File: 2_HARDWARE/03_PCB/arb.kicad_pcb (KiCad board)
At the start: 4 copper layers, 100 x 100 mm, 268 parts, among them J1 TYPE-C-31-M-12, J2 SMA, J3 SMA, J4 BNC, J5 PH-00244, SW1 TS-1187A-B-A-B, SW2 SS-12D02-VG4, SW3 SS-12D02-VG4, U1 TLV70333DBV, U10 LMK1C1103PWR, U11 STM32F446ZETx, U12 ICE40UP5K-SG48ITR, U13 93LC56BT-I_OT, U14 FT2232HL, U15 W25Q128JVSIQ, U16 W25Q128JVSIQ, U17 AD9850, U18 AD9744, U19 LM6171, U2 TLV76133DCY, U20 LM6171, U21 TMUX6104, U22 TPL0401B-10, U23 THS3491, U24 ADG1219BRJZ, U25 LM6171, U26 TMUX6104, U3 TLV70333DBV, U4 LM3880MF-1AA, U5 TLV70312DBV, U6 TLV70325DBV, U7 TPS65131RGE, U8 TPD2E001DRL, U9 ADG1219BRJZ, X1 ASE-10.000MHz, X2 ASE-100.000MHz, Y1 32.768k, Y2 12 MHz

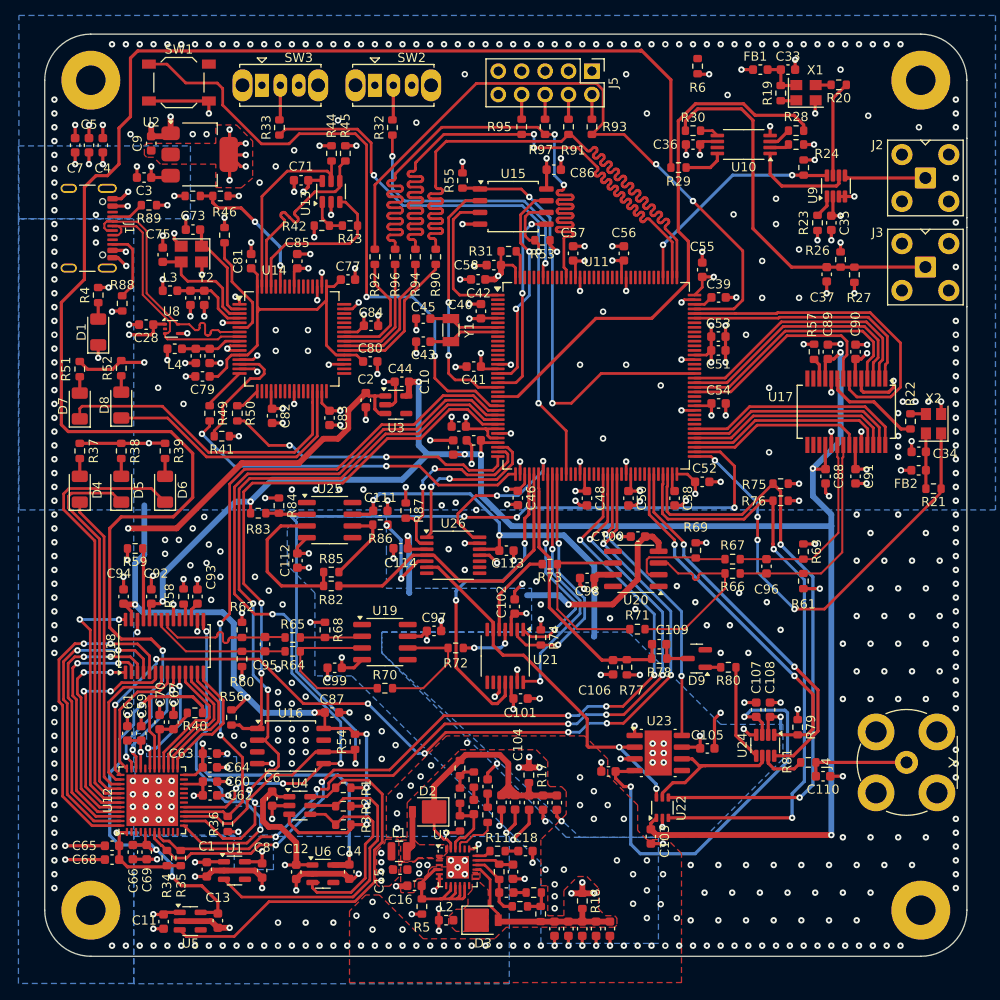
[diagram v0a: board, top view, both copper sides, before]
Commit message: FEAT: Added silkscreen.
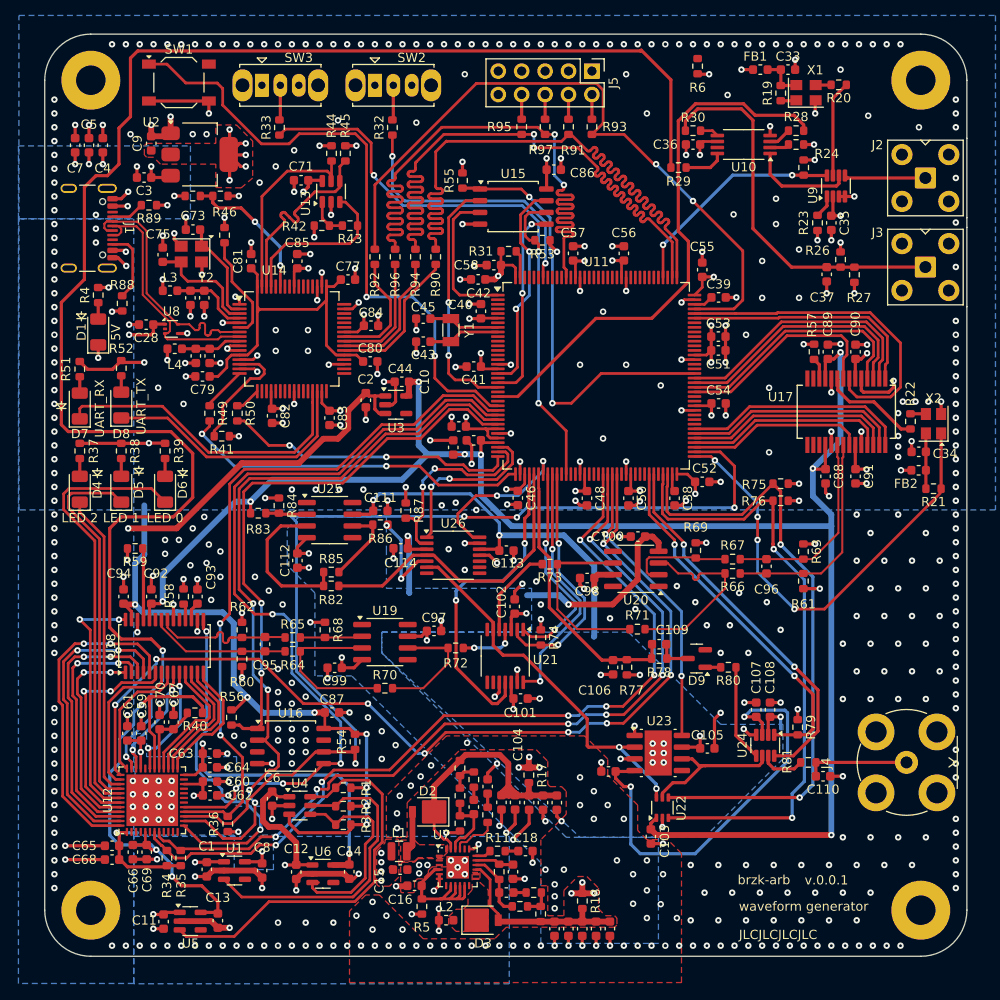
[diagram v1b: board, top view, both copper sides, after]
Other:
- board text added: "5V"
- board text added: "JLCJLCJLCJLC"
- board text added: "LED 0"
- board text added: "LED 1"
- board text added: "LED 2"
- board text added: "UART_RX"
- board text added: "UART_TX"
- board text added: "brzk-arb"
- board text added: "v.0.0.1"
- board text added: "waveform generator"

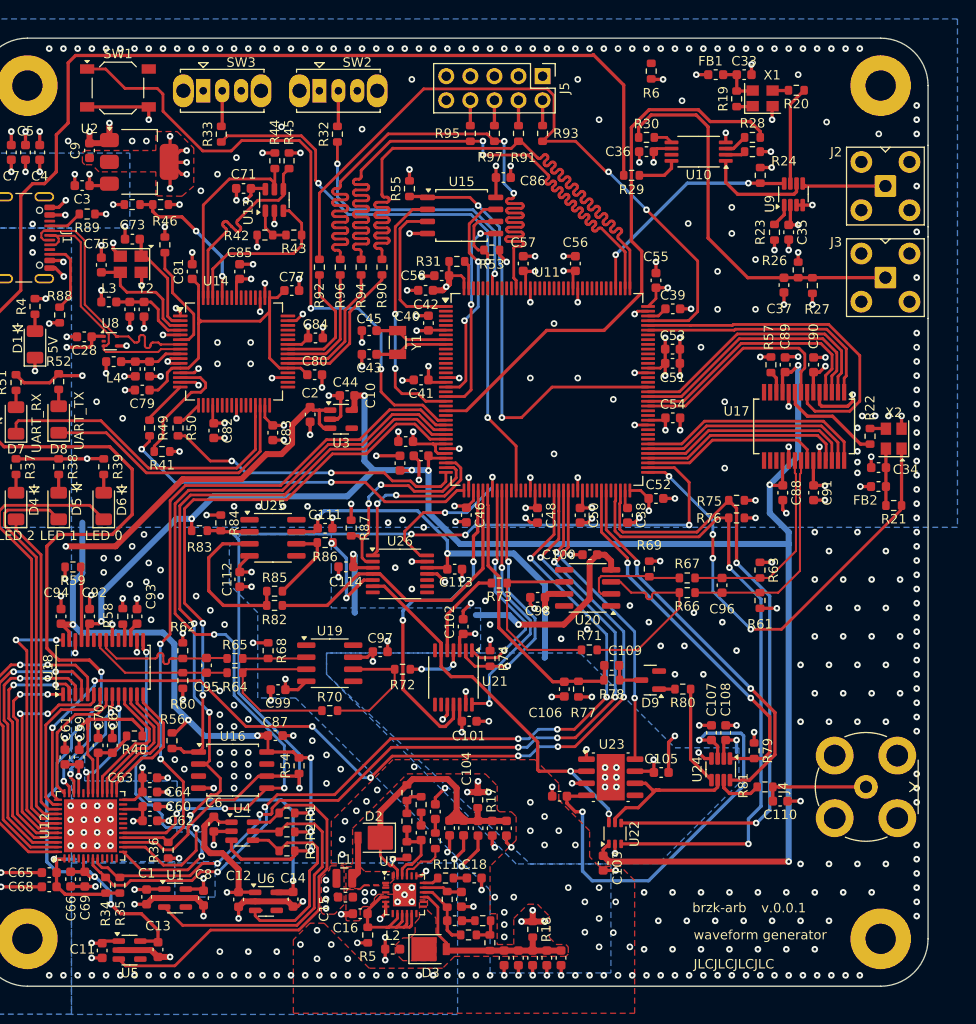
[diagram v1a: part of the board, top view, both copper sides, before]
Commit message: MINOR: Adjusted soldermask and ported Schematic + PCB to Kicad 9.0.
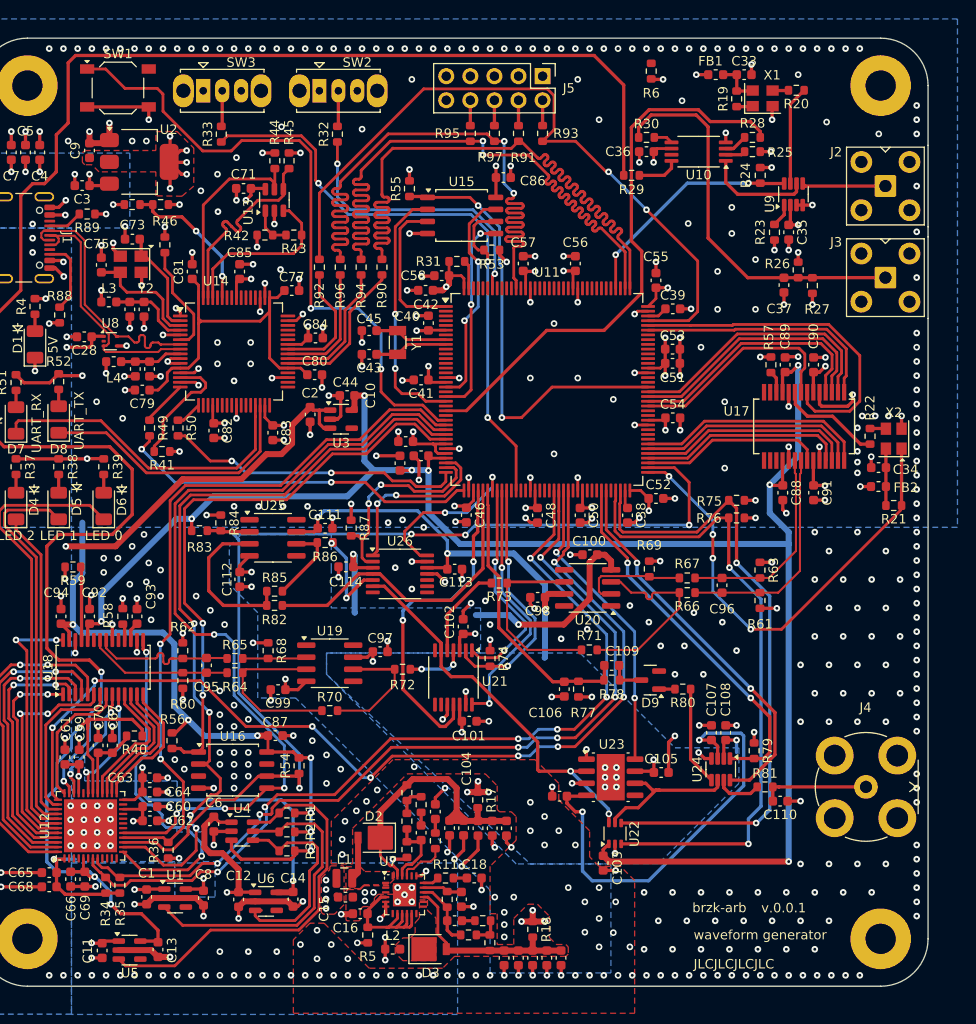
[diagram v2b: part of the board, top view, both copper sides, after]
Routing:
- net GND: vias 613 -> 616

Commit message: MINOR: Initial Reduced Size Analysis, need to make the board larger.
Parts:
- J2, J3, J4, U11: moved to B.Cu
- moved C1 351.3 mm to (-231.4, 99.1)
- moved C10 351.3 mm to (-210.2, 46.2)
- moved C100 351.3 mm to (-184.6, 63.0)
- moved C101 351.3 mm to (-197.3, 80.5)
- moved C102 351.3 mm to (-198.0, 70.6)
- moved C103 351.3 mm to (-183.2, 95.5)
- moved C104 351.3 mm to (-187.8, 88.5)
- moved C105 351.3 mm to (-177.1, 86.0)
- moved C106 351.3 mm to (-187.3, 77.2)
- moved C107 351.3 mm to (-171.8, 81.8)
- moved C108 351.3 mm to (-170.3, 81.8)
- moved C109 351.3 mm to (-182.3, 74.7)
- moved C11 351.3 mm to (-236.1, 104.7)
- moved C110 351.3 mm to (-164.6, 89.0)
- moved C111 351.3 mm to (-212.6, 60.2)
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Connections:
- J1 pad A1: GND -> (no net)
- J1 pad A12: GND -> (no net)
- J1 pad A4: 5P0V -> (no net)
- J1 pad A5: Net-(J1-CC1) -> (no net)
- J1 pad A6: USB_DATA_CONN_FTDI_P -> (no net)
- J1 pad A7: USB_DATA_CONN_FTDI_N -> (no net)
- J1 pad A8: unconnected-(J1-SBU1-PadA8) -> (no net)
- J1 pad A9: 5P0V -> (no net)
- J1 pad B1: GND -> (no net)
- J1 pad B12: GND -> (no net)
- J1 pad B4: 5P0V -> (no net)
- J1 pad B5: Net-(J1-CC2) -> (no net)
- J1 pad B6: USB_DATA_CONN_FTDI_P -> (no net)
- J1 pad B7: USB_DATA_CONN_FTDI_N -> (no net)
- J1 pad B8: unconnected-(J1-SBU2-PadB8) -> (no net)
- J1 pad B9: 5P0V -> (no net)
- J1 pad S1: GND -> (no net)
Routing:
- net GND: track 298.4 -> 0.00 mm, vias 616 -> 0
- net 3P3V_D: track 211.8 -> 0.00 mm, vias 54 -> 0
- net 3P3V_A: track 190.5 -> 0.00 mm, vias 8 -> 0
- net CLK_10MHZ_DIST_FPGA_3P3: track 176.2 -> 0.00 mm, vias 2 -> 0
- net SPI_SCLK_MCU_FPGA_3P3: track 112.0 -> 0.00 mm, vias 4 -> 0
- net GPIO_CLK_EN_MCU_FPGA_3P3: track 103.8 -> 0.00 mm, vias 8 -> 0
- net GPIO_CFG_DONE_FPGA_MCU_3P3: track 91.5 -> 0.00 mm, vias 6 -> 0
- net N15P0V_A: track 91.4 -> 0.00 mm, vias 10 -> 0
- net GPIO_FPGARST_MCU_FPGA_3P3_L: track 90.4 -> 0.00 mm, vias 6 -> 0
- net SPI_MOSI_MCU_FPGA_3P3: track 89.2 -> 0.00 mm, vias 4 -> 0
- net SPI_MISO_FPGA_MCU_3P3: track 82.8 -> 0.00 mm, vias 4 -> 0
- net 5P0V: track 80.5 -> 0.00 mm, vias 19 -> 0
- net SPI_CS_MCU_FPGA_3P3_L: track 76.9 -> 0.00 mm, vias 2 -> 0
- net JTAG_MCU_TDI_3P3: track 75.2 -> 0.00 mm, vias 2 -> 0
- net JTAG_MCU_TMS_3P3: track 74.5 -> 0.00 mm, vias 2 -> 0
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- removed copper zone on B.Cu, net 15P0V_A
- removed copper zone on B.Cu, net 3P3V_D
- removed copper zone on F.Cu, net 3P3V_D
- removed copper zone on B.Cu, net 3P3V_D_FPGA
- removed copper zone on B.Cu, net 5P0V
- removed copper zone on F.Cu, net 5P0V
- removed copper zone on F.Cu, net GND
- removed copper zone on B.Cu, net N15P0V_A
- removed copper zone on F.Cu, net Net-(D2-A)
- removed copper zone on F.Cu, net Net-(D3-K)
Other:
- board size 100 x 100 mm -> 44.6 x 44.6 mm
- board text added: "v.1.0.1"
- board text removed: "v.0.0.1"

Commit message: MINOR: Changed board outline and started component placement.
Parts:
- added R98: 0, Resistor_SMD:R_0603_1608Metric, B.Cu at (29.6, 175.2)
- C10, C100, C101, C102, C103, C104, C105, C106, C107, C108, C109, C110, C111, C112, C113, C114, C15, C16, C17, C18, C19, C2, C20, C21, C22, C23, C24, C25, C26, C27, C29, C30, C31, C32, C72, C76, C95, C96, C97, C98, C99, D2, D3, D9, L1, L2, L3, R10, R11, R12, R13, R14, R15, R16, R17, R18, R5, R60, R61, R62, R63, R64, R65, R66, R67, R68, R69, R7, R70, R71, R72, R73, R74, R75, R76, R77, R78, R79, R8, R80, R81, R82, R83, R84, R85, R86, R87, R9, U19, U20, U21, U22, U23, U24, U25, U26, U3, U7: moved to B.Cu
- H1, H2, H3, H4: footprint MountingHole:MountingHole_3.2mm_M3_Pad -> MountingHole:MountingHole_3.2mm_M3_Pad_Via
- J2, J3, J4, U11: moved to F.Cu
- R6: value 1M -> 0; moved to B.Cu
- moved C34 392.1 mm to (237.7, 66.3)
- moved FB2 392.1 mm to (237.7, 68.3)
- moved R21 392.1 mm to (239.3, 70.3)
- moved R22 392.1 mm to (236.8, 63.0)
- moved X2 392.1 mm to (239.3, 63.2)
- moved R59 387.9 mm to (146.8, 103.4), turned to 90 degrees
- moved D4 386.7 mm to (131.5, 145.4)
- moved D5 386.7 mm to (136.0, 145.4)
- moved D6 386.7 mm to (140.8, 145.4)
- moved R37 386.7 mm to (131.5, 141.2)
- moved R38 386.7 mm to (136.0, 141.2)
- moved R39 386.7 mm to (140.8, 141.2)
- moved C94 383.4 mm to (141.6, 102.1), turned to 0 degrees
- moved C92 380.7 mm to (141.6, 105.1), turned to 0 degrees
- moved R58 377.5 mm to (141.6, 108.6), turned to 0 degrees
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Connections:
- J1 pad A1: (no net) -> GND
- J1 pad A12: (no net) -> GND
- J1 pad A4: (no net) -> 5P0V
- J1 pad A5: (no net) -> Net-(J1-CC1)
- J1 pad A6: (no net) -> USB_DATA_CONN_FTDI_P
- J1 pad A7: (no net) -> USB_DATA_CONN_FTDI_N
- J1 pad A8: (no net) -> unconnected-(J1-SBU1-PadA8)
- J1 pad A9: (no net) -> 5P0V
- J1 pad B1: (no net) -> GND
- J1 pad B12: (no net) -> GND
- J1 pad B4: (no net) -> 5P0V
- J1 pad B5: (no net) -> Net-(J1-CC2)
- J1 pad B6: (no net) -> USB_DATA_CONN_FTDI_P
- J1 pad B7: (no net) -> USB_DATA_CONN_FTDI_N
- J1 pad B8: (no net) -> unconnected-(J1-SBU2-PadB8)
- J1 pad B9: (no net) -> 5P0V
- J1 pad S1: (no net) -> GND
- R6 pad 1: C_GND -> ANALOG_DC-OFFSET_AMUX3_AMP3
- R6 pad 2: GND -> Net-(R6-Pad2)
- U22 pad 6: ANALOG_DC-OFFSET_AMUX3_AMP3 -> Net-(U22-H)
- U23 pad 2: ANALOG_DC-OFFSET_AMUX3_AMP3 -> Net-(U22-H)
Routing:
- net ANALOG_FPGA-DAC_OUT_N: track 7.64 -> 0.00 mm
- net USB_DATA_CONN_FTDI_N: track 4.31 -> 0.00 mm
- net Net-(U20-+): track 3.38 -> 0.00 mm
- net Net-(U13-CLK): track 2.16 -> 0.00 mm
- net GND: vias 0 -> 221
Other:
- board size 44.6 x 44.6 mm -> 104.3 x 53.5 mm

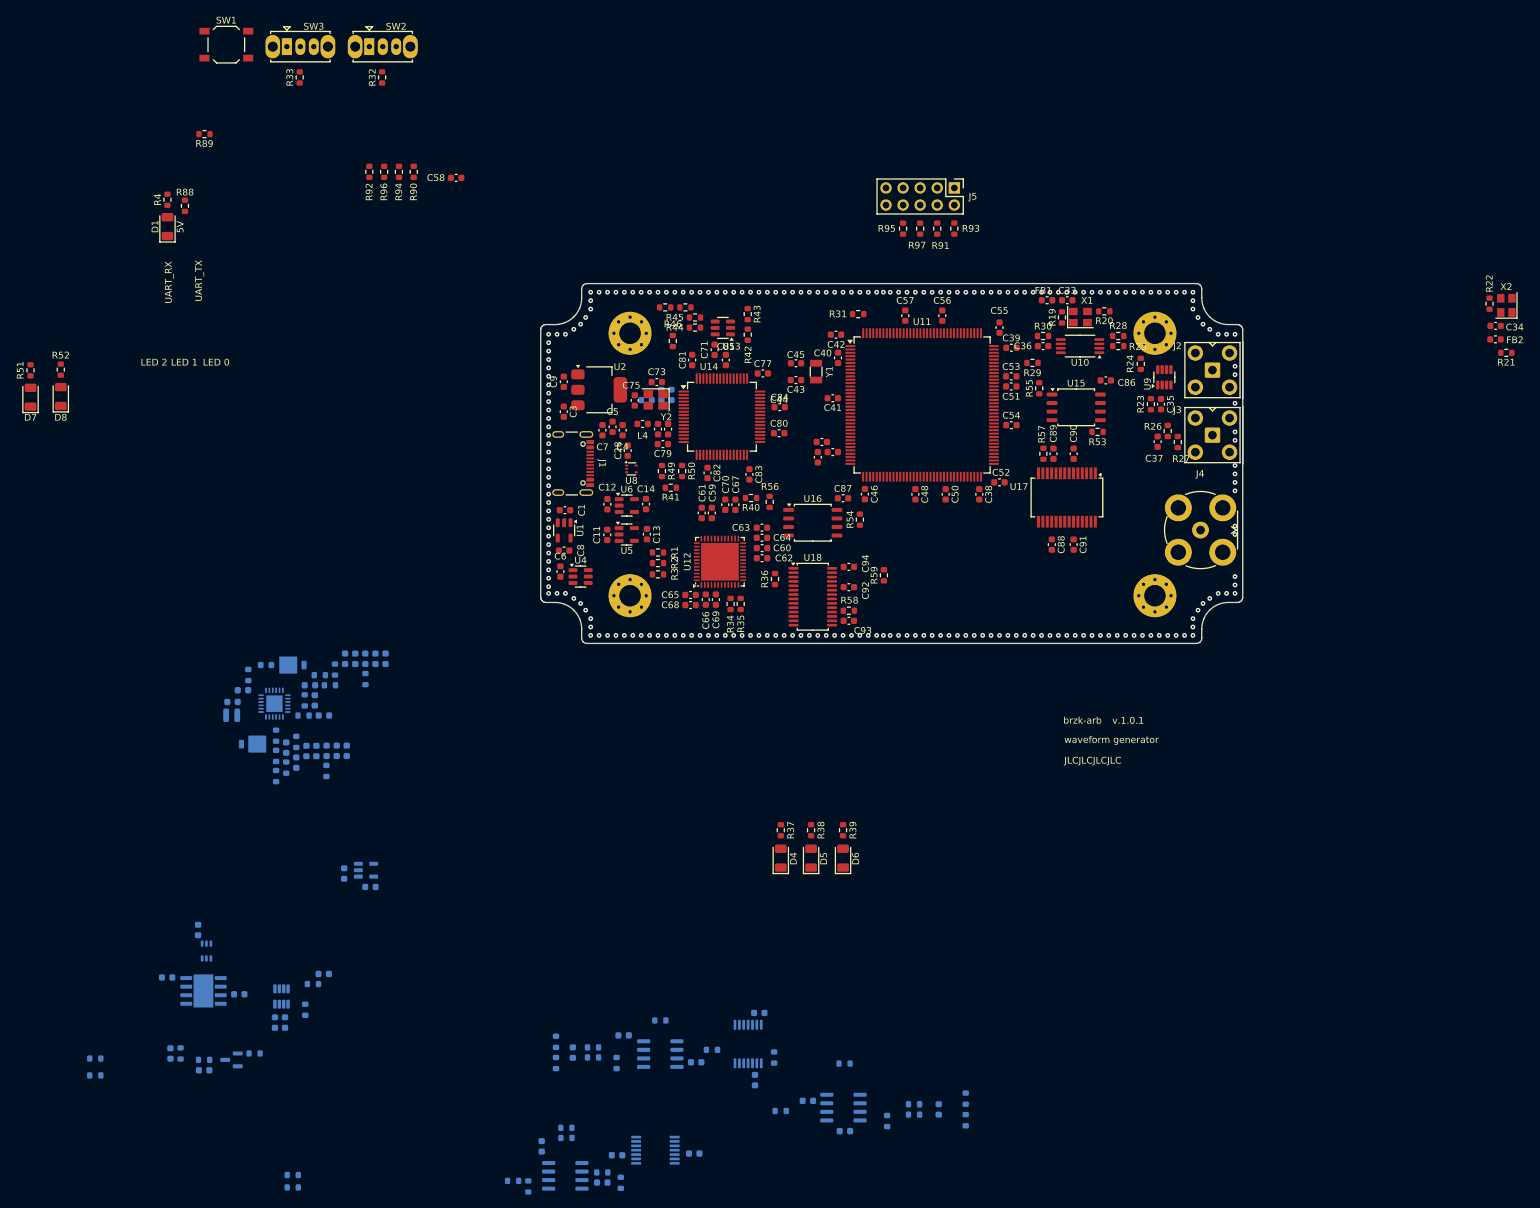
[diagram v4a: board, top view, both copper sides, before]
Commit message: MINOR: Changed Boot Select Switches to Pull-Downs / Pull Up DNI and continued layout.
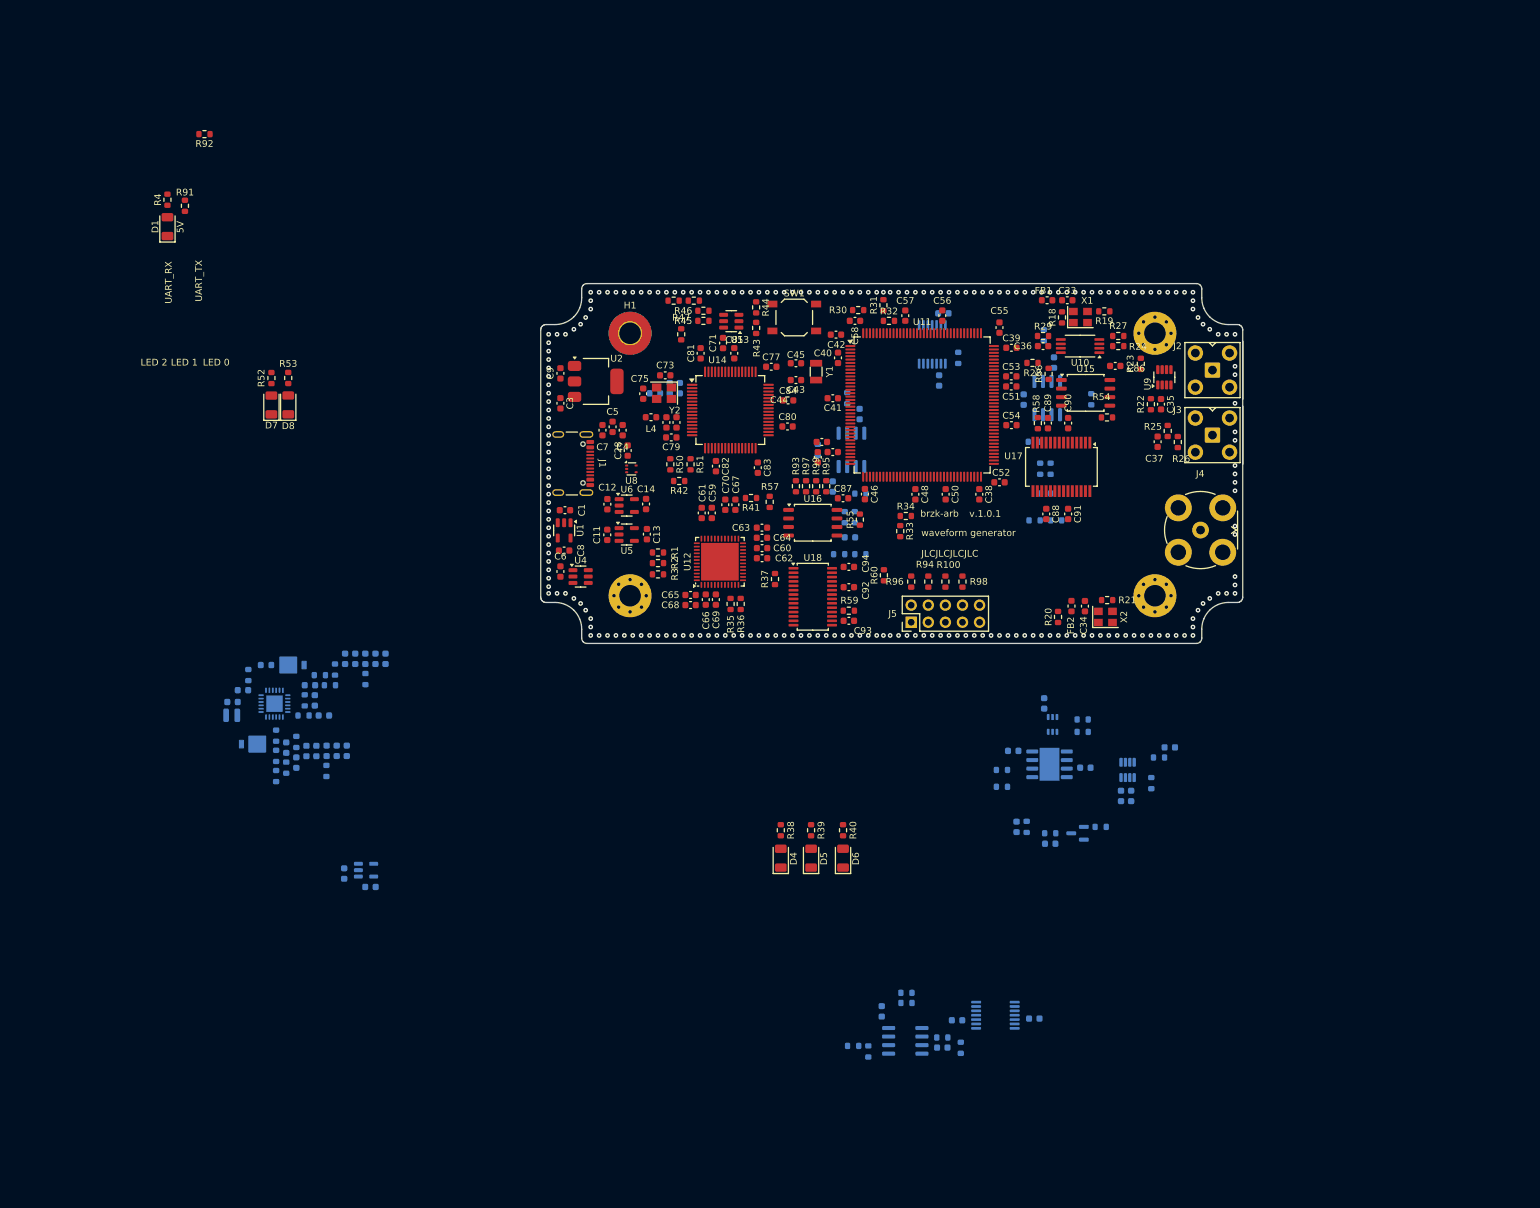
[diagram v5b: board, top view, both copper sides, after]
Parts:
- removed SW2, SW3: SS-12D02-VG4, BRZK_SW:SW_TH_Slide_SPDT_Straight_SS-12D02-VG4
- added R31: 10k, Resistor_SMD:R_0603_1608Metric, F.Cu at (146.8, 63.2)
- added R34: 10k, Resistor_SMD:R_0603_1608Metric, F.Cu at (150.1, 94.5)
- H1: footprint MountingHole:MountingHole_3.2mm_M3_Pad_Via -> MountingHole:MountingHole_3.2mm_M3_Pad_TopBottom
- moved R78 141.4 mm to (164.4, 134.8)
- moved R79 141.4 mm to (164.4, 132.3)
- moved R76 135.5 mm to (176.4, 126.6)
- moved R77 135.5 mm to (176.4, 124.8)
- moved C110 130.2 mm to (189.3, 128.9)
- moved R84 130.2 mm to (187.7, 130.4)
- moved C103 130.2 mm to (170.6, 122.4)
- moved C104 130.2 mm to (166.0, 129.5)
- moved C105 130.2 mm to (176.8, 132.0)
- moved C106 130.2 mm to (166.5, 140.8)
- moved C107 130.2 mm to (182.1, 136.2)
- moved C108 130.2 mm to (183.6, 136.2)
- moved C109 130.2 mm to (171.5, 143.2)
- moved D9 130.2 mm to (175.6, 141.7)
- moved R80 130.2 mm to (168.0, 140.8)
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- renumbered R11 to R10, R97 to R100, R12 to R11, R13 to R12, R14 to R13, R15 to R14, R16 to R15, R17 to R16, R18 to R17, R19 to R18, R20 to R19, R21 to R20, R22 to R21, R23 to R22, R24 to R23, R25 to R24, R26 to R25, R27 to R26, R28 to R27, R29 to R28, R30 to R29, R31 to R30, R34 to R35, R35 to R36, R36 to R37, R37 to R38, R38 to R39, R39 to R40, R40 to R41, R41 to R42, R42 to R43, R43 to R44, R44 to R45, R45 to R46, R46 to R47, R47 to R48, R48 to R49, R49 to R50, R50 to R51, R51 to R52, R52 to R53, R53 to R54, R54 to R55, R55 to R56, R56 to R57, R57 to R58, R58 to R59, R7 to R6, R59 to R60, R60 to R61, R61 to R62, R62 to R63, R63 to R64, R64 to R65, R65 to R66, R66 to R67, R67 to R68, R68 to R69, R8 to R7, R69 to R70, R70 to R71, R71 to R72, R72 to R73, R73 to R74, R74 to R75, R75 to R76, R76 to R77, R6 to R78, R98 to R79, R9 to R8, R77 to R80, R78 to R81, R79 to R82, R80 to R83, R81 to R84, R82 to R85, R83 to R86, R84 to R87, R85 to R88, R86 to R89, R10 to R9, R87 to R90, R88 to R91, R89 to R92, R90 to R93, R91 to R94, R92 to R95, R93 to R96, R94 to R97, R95 to R98, R96 to R99
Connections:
- R32 pad 2: Net-(SW2-COM) -> GND
- R33 pad 2: Net-(SW3-COM) -> 3P3V_D
